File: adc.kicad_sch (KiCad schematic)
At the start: 97 parts, among them U18 TLV9004IPWR, U22 TLV9004IPWR, U8 TLA2518IRTER

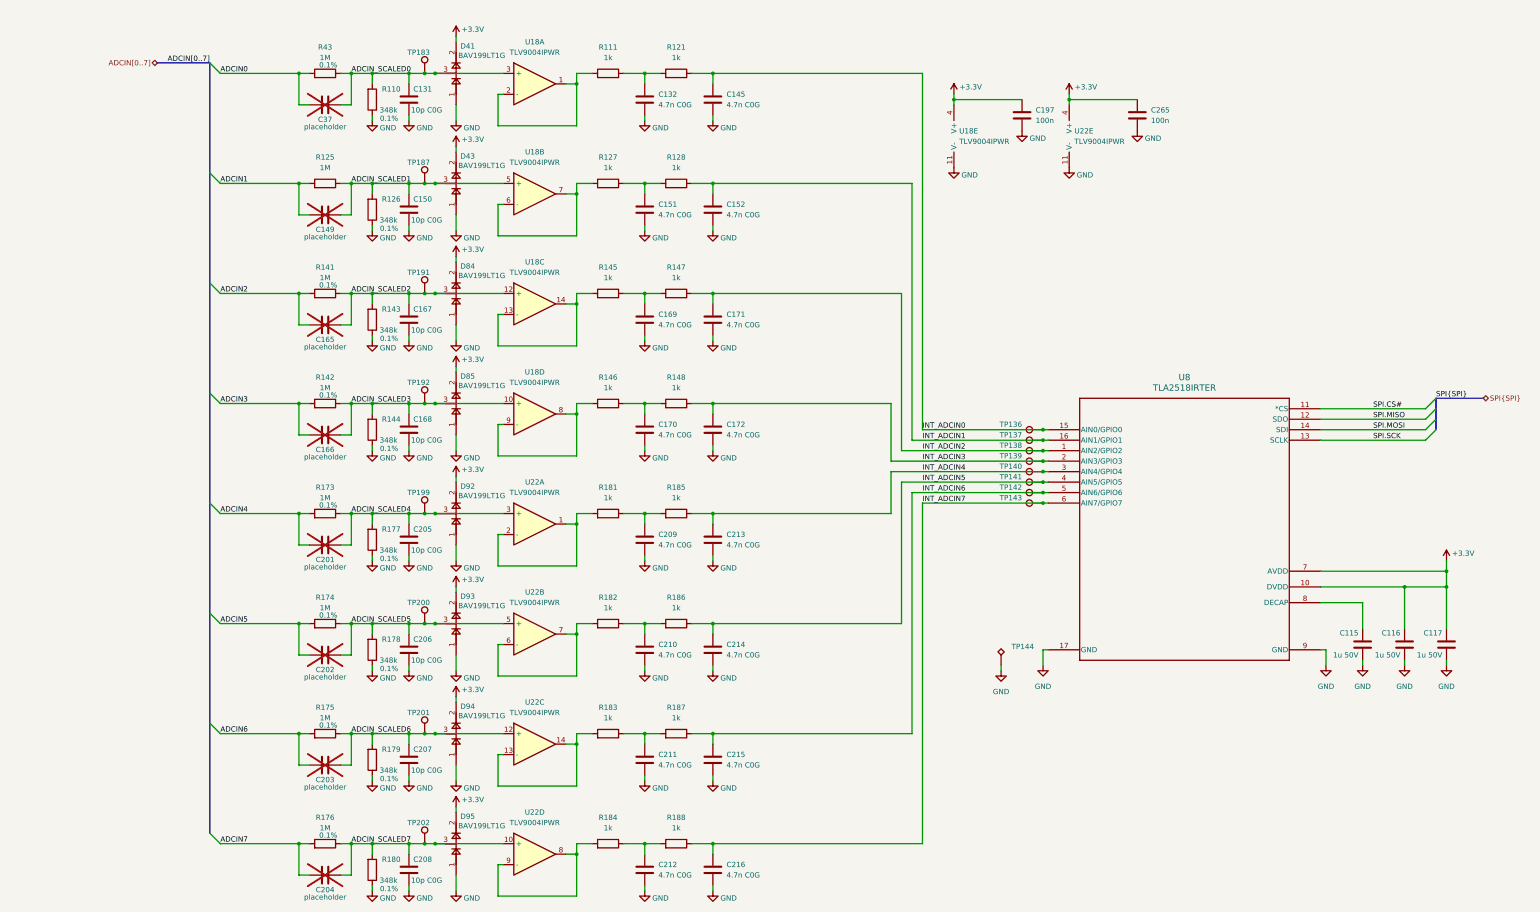
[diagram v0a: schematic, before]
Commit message: fixed some issues, preliminary layout on adc input filter/scaling
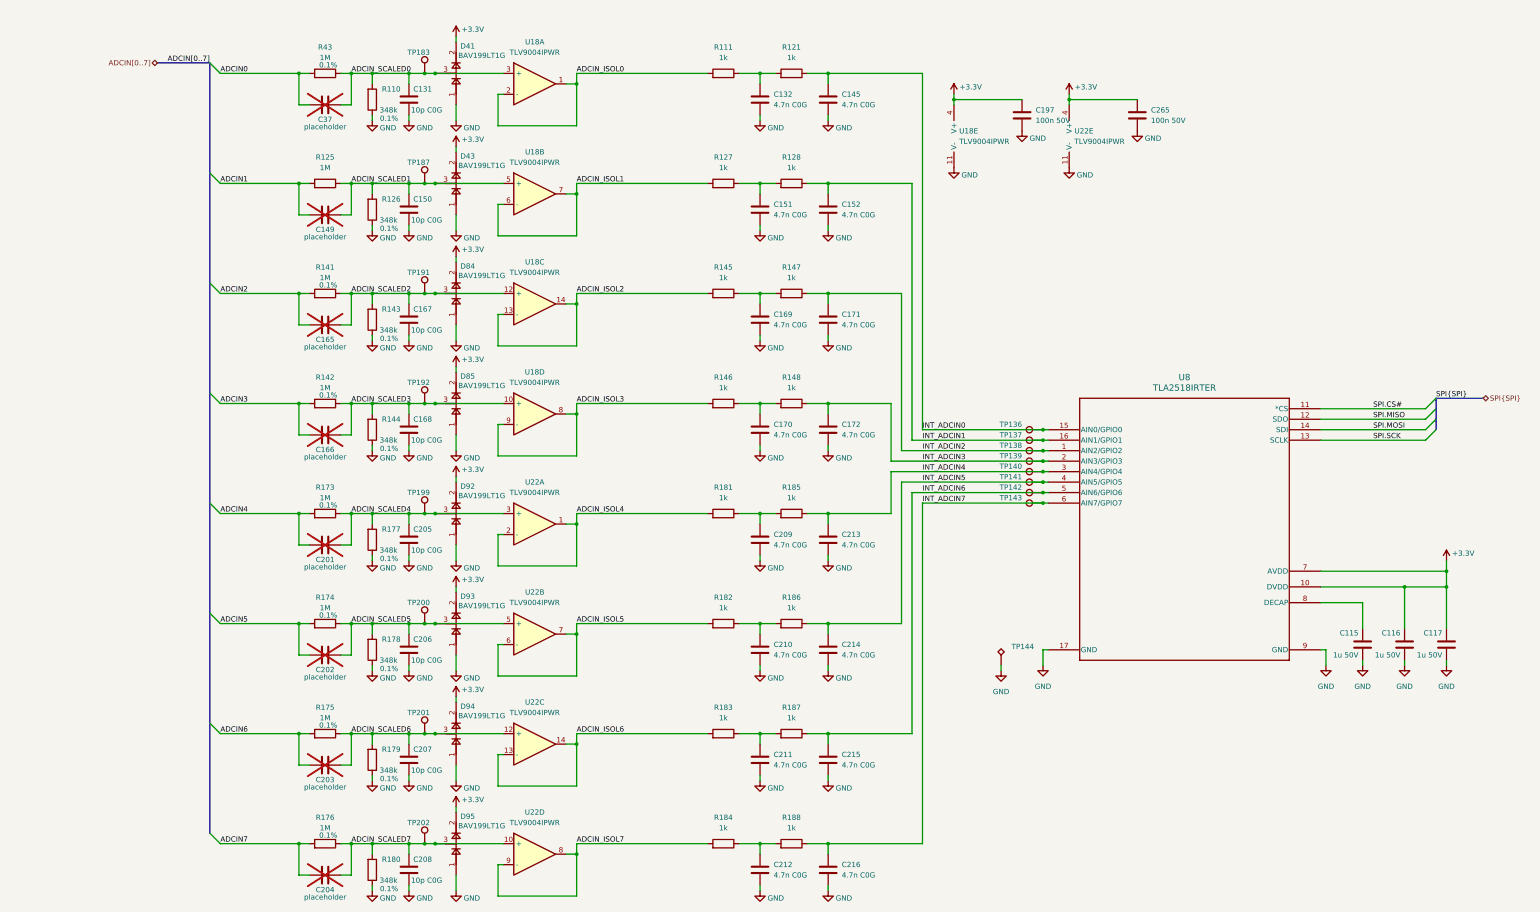
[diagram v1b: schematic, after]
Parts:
- C149, C165, C166, C201, C202, C203, C204, C37: footprint (none) -> Capacitor_SMD:C_0402_1005Metric
- C197, C265: value 100n -> 100n 50V; footprint (none) -> Capacitor_SMD:C_0402_1005Metric; LCSC (none) -> C307331; LCSC Basic/Pref (none) -> x; LCSC Part (none) -> C307331
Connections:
- net ADCIN_ISOL5: now reaches R182.2, U22.6 (-), U22.7
- net ADCIN_ISOL3: now reaches R146.2, U18.8, U18.9 (-)
- net ADCIN_ISOL2: now reaches R145.2, U18.13 (-), U18.14
- net ADCIN_ISOL4: now reaches R181.2, U22.1, U22.2 (-)
- net ADCIN_ISOL7: now reaches R184.2, U22.8, U22.9 (-)
- net ADCIN_ISOL6: now reaches R183.2, U22.13 (-), U22.14
- net ADCIN_ISOL1: now reaches R127.2, U18.6 (-), U18.7
- net ADCIN_ISOL0: now reaches R111.2, U18.1, U18.2 (-)
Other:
- moved on the sheet: C132, C145, C151, C152, C169, C170, C171, C172, C209, C210, C211, C212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

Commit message: did some placement/routing of adc input stage
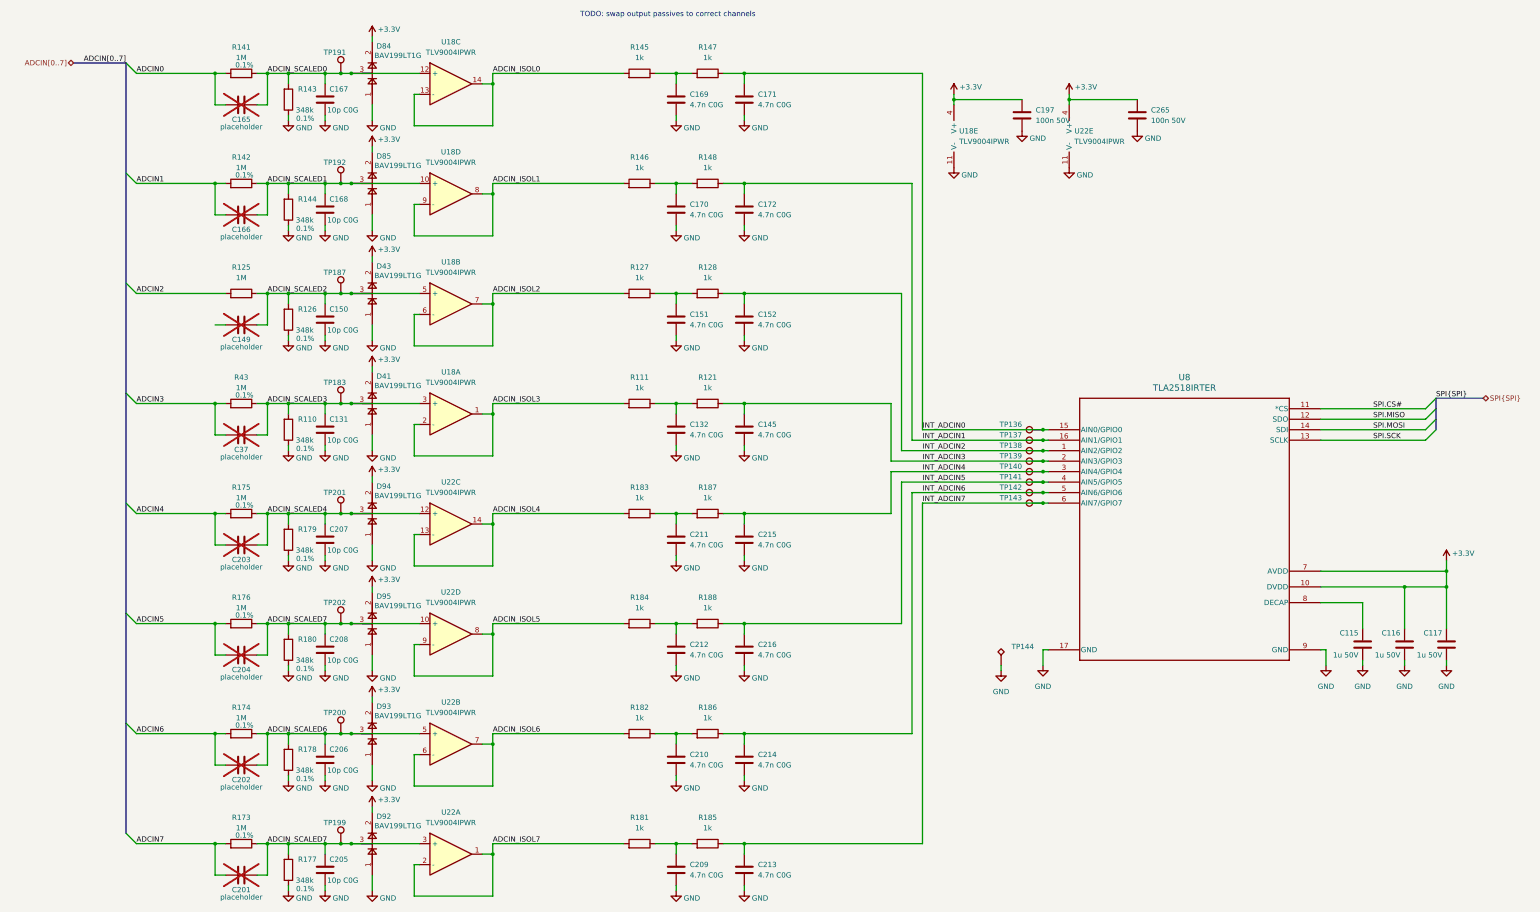
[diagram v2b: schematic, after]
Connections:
- net ADCIN_SCALED5 is gone; now on net ADCIN_SCALED6: C202.1, C206.2, D93.3, R174.1, R178.2, TP200.1, U22.5 (+)
- net ADCIN0: now also C165.2, R141.2; no longer C37.2, R43.2
- net ADCIN1: now also C166.2, R142.2; no longer C149.2, R125.2
- net ADCIN2: now also R125.2; no longer C165.2, R141.2
- net ADCIN3: now also C37.2, R43.2; no longer C166.2, R142.2
- net ADCIN4: now also C203.2, R175.2; no longer C201.2, R173.2
- net ADCIN5: now also C204.2, R176.2; no longer C202.2, R174.2
- net ADCIN6: now also C202.2, R174.2; no longer C203.2, R175.2
- net ADCIN7: now also C201.2, R173.2; no longer C204.2, R176.2
- net ADCIN_ISOL0: now also R145.2, U18.13 (-), U18.14; no longer R111.2, U18.1, U18.2 (-)
- net ADCIN_ISOL1: now also R146.2, U18.8, U18.9 (-); no longer R127.2, U18.6 (-), U18.7
- net ADCIN_ISOL2: now also R127.2, U18.6 (-), U18.7; no longer R145.2, U18.13 (-), U18.14
- net ADCIN_ISOL3: now also R111.2, U18.1, U18.2 (-); no longer R146.2, U18.8, U18.9 (-)
- net ADCIN_ISOL4: now also R183.2, U22.13 (-), U22.14; no longer R181.2, U22.1, U22.2 (-)
- net ADCIN_ISOL5: now also R184.2, U22.8, U22.9 (-); no longer R182.2, U22.6 (-), U22.7
- net ADCIN_ISOL6: now also R182.2, U22.6 (-), U22.7; no longer R183.2, U22.13 (-), U22.14
- net ADCIN_ISOL7: now also R181.2, U22.1, U22.2 (-); no longer R184.2, U22.8, U22.9 (-)
- net ADCIN_SCALED0: now also C165.1, C167.2, D84.3, R141.1, R143.2, TP191.1, U18.12 (+); no longer C131.2, C37.1, D41.3, R110.2, R43.1, TP183.1, U18.3 (+)
- net ADCIN_SCALED1: now also C166.1, C168.2, D85.3, R142.1, R144.2, TP192.1, U18.10 (+); no longer C149.1, C150.2, D43.3, R125.1, R126.2, TP187.1, U18.5 (+)
- net ADCIN_SCALED2: now also C149.1, C150.2, D43.3, R125.1, R126.2, TP187.1, U18.5 (+); no longer C165.1, C167.2, D84.3, R141.1, R143.2, TP191.1, U18.12 (+)
- net ADCIN_SCALED3: now also C131.2, C37.1, D41.3, R110.2, R43.1, TP183.1, U18.3 (+); no longer C166.1, C168.2, D85.3, R142.1, R144.2, TP192.1, U18.10 (+)
- net ADCIN_SCALED4: now also C203.1, C207.2, D94.3, R175.1, R179.2, TP201.1, U22.12 (+); no longer C201.1, C205.2, D92.3, R173.1, R177.2, TP199.1, U22.3 (+)
- net ADCIN_SCALED6: no longer C203.1, C207.2, D94.3, R175.1, R179.2, TP201.1, U22.12 (+)
- net ADCIN_SCALED7: now also C201.1, C205.2, D92.3, R173.1, R177.2, TP199.1, U22.3 (+)
- net INT_ADCIN0: now also C171.2, R147.1; no longer C145.2, R121.1
- net INT_ADCIN1: now also C172.2, R148.1; no longer C152.2, R128.1
- net INT_ADCIN2: now also C152.2, R128.1; no longer C171.2, R147.1
- net INT_ADCIN3: now also C145.2, R121.1; no longer C172.2, R148.1
- net INT_ADCIN4: now also C215.2, R187.1; no longer C213.2, R185.1
- net INT_ADCIN5: now also C216.2, R188.1; no longer C214.2, R186.1
- net INT_ADCIN6: now also C214.2, R186.1; no longer C215.2, R187.1
- net INT_ADCIN7: now also C213.2, R185.1; no longer C216.2, R188.1
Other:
- note added: "TODO: swap output passives to correct channels"
- moved on the sheet: C131, C132, C145, C201, C202, C204, C205, C206, C208, C209, C210, C212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

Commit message: did stuff
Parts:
- D41, D43, D84, D85, D92, D93, D94, D95: LCSC (none) -> C145516
- R111, R121, R127, R128, R145, R146, R147, R148, R181, R182, R183, R184, R185, R186, R187, R188: LCSC Basic/Pref x -> y
- U18, U22: LCSC (none) -> C2058050
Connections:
- net ADCIN_ISOL0: now also R111.2; no longer R145.2
- net ADCIN_ISOL1: now also R127.2; no longer R146.2
- net ADCIN_ISOL2: now also R145.2; no longer R127.2
- net ADCIN_ISOL3: now also R146.2; no longer R111.2
- net ADCIN_ISOL4: now also R181.2; no longer R183.2
- net ADCIN_ISOL5: now also R182.2; no longer R184.2
- net ADCIN_ISOL6: now also R183.2; no longer R182.2
- net ADCIN_ISOL7: now also R184.2; no longer R181.2
- net ADCIN_SCALED7: no longer C204.1, C208.2, D95.3, R176.1, R180.2, TP202.1, U22.10 (+)
- net INT_ADCIN0: now also C145.2, R121.1; no longer C171.2, R147.1
- net INT_ADCIN1: now also C152.2, R128.1; no longer C172.2, R148.1
- net INT_ADCIN2: now also C171.2, R147.1; no longer C152.2, R128.1
- net INT_ADCIN3: now also C172.2, R148.1; no longer C145.2, R121.1
- net INT_ADCIN4: now also C213.2, R185.1; no longer C215.2, R187.1
- net INT_ADCIN5: now also C214.2, R186.1; no longer C216.2, R188.1
- net INT_ADCIN6: now also C215.2, R187.1; no longer C214.2, R186.1
- net INT_ADCIN7: now also C216.2, R188.1; no longer C213.2, R185.1
- new net ADCIN_SCALED5: C204.1, C208.2, D95.3, R176.1, R180.2, TP202.1, U22.10 (+)
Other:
- note removed: "TODO: swap output passives to correct channels"
- moved on the sheet: C132, C145, C151, C152, C169, C170, C171, C172, C209, C210, C211, C212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

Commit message: fixed a lot of review comments
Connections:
- net ADCIN2: now also C149.2
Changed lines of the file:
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@@
+	)
+	(junction
+		(at 74.93 87.63)
+		(diameter 0)
+		(color 0 0 0 0)
 	)
 	(junction
@@
 	(wire
 		(pts
+			(xy 74.93 87.63) (xy 74.93 95.25)
+		)
+		(stroke
+			(width 0)
+			(type default)
+		)
+	)
+	(wire
+		(pts
 			(xy 281.94 40.64) (xy 298.45 40.64)
 		)
@@
 	(wire
 		(pts
+			(xy 74.93 87.63) (xy 77.47 87.63)
+		)
+		(stroke
+			(width 0)
+			(type default)
+		)
+	)
+	(wire
+		(pts
 			(xy 55.88 194.31) (xy 74.93 194.31)
 		)
@@
 	(wire
 		(pts
-			(xy 55.88 87.63) (xy 77.47 87.63)
-		)
-		(stroke
+			(xy 55.88 87.63) (xy 74.93 87.63)
+		)
+		(stroke

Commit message: pre-changing properties
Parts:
- C132, C145, C151, C152, C169, C170, C171, C172, C209, C210, C211, C212, C213, C214, C215, C216: value 4.7n C0G -> 33n C0G; footprint Resistor_SMD:R_0402_1005Metric -> Resistor_SMD:R_0805_2012Metric; LCSC C1518204 -> C76628; LCSC Part C1518204 -> C76628; Tolerance (none) -> 5%; Voltage (none) -> 50V
- C149, C165, C166, C201, C202, C203, C204, C37: now left out of the parts list
- R111, R121, R127, R128, R145, R146, R147, R148, R181, R182, R183, R184, R185, R186, R187, R188: value 1k -> 100; LCSC C11702 -> C25076; LCSC Part C11702 -> C25076; LCSC missing (none) -> n; MPN (none) -> 0402WGF1000TCE; Manufacturer (none) -> UNI-ROYAL(Uniroyal Elec); Power (none) -> 62.5mW; Tolerance (none) -> 1%; Voltage (none) -> 50V
- U8: footprint WQFN16_RTE_TEX -> TLA2518IRTER:WQFN16_RTE_TEX
